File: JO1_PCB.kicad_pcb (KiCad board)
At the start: 2 copper layers, 118.1 x 90.2 mm, 5 parts, among them J1 Conn_02x10_Row_Letter_First, J2 Conn_02x08_Row_Letter_First, J3 Conn_02x15_Row_Letter_First, J4 Conn_02x17_Row_Letter_First

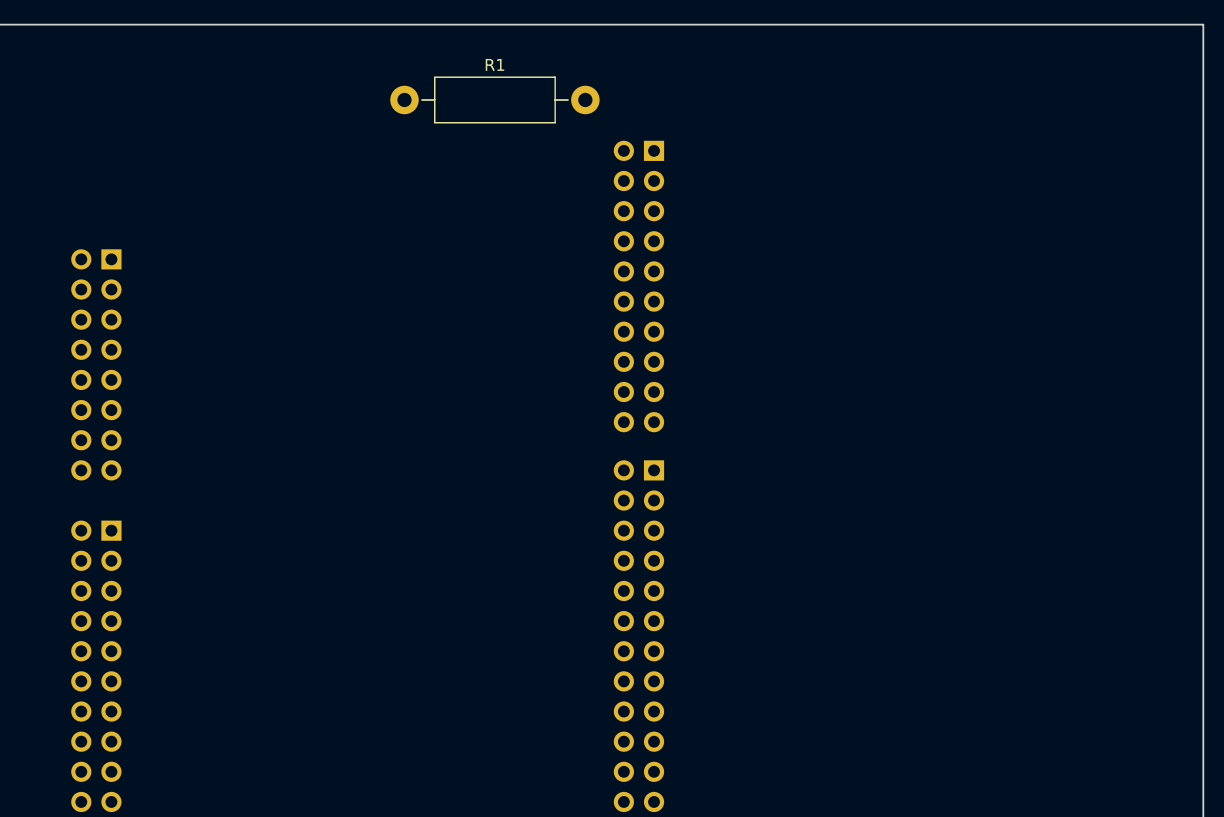
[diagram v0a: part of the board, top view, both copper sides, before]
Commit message: Added several components to the schematic
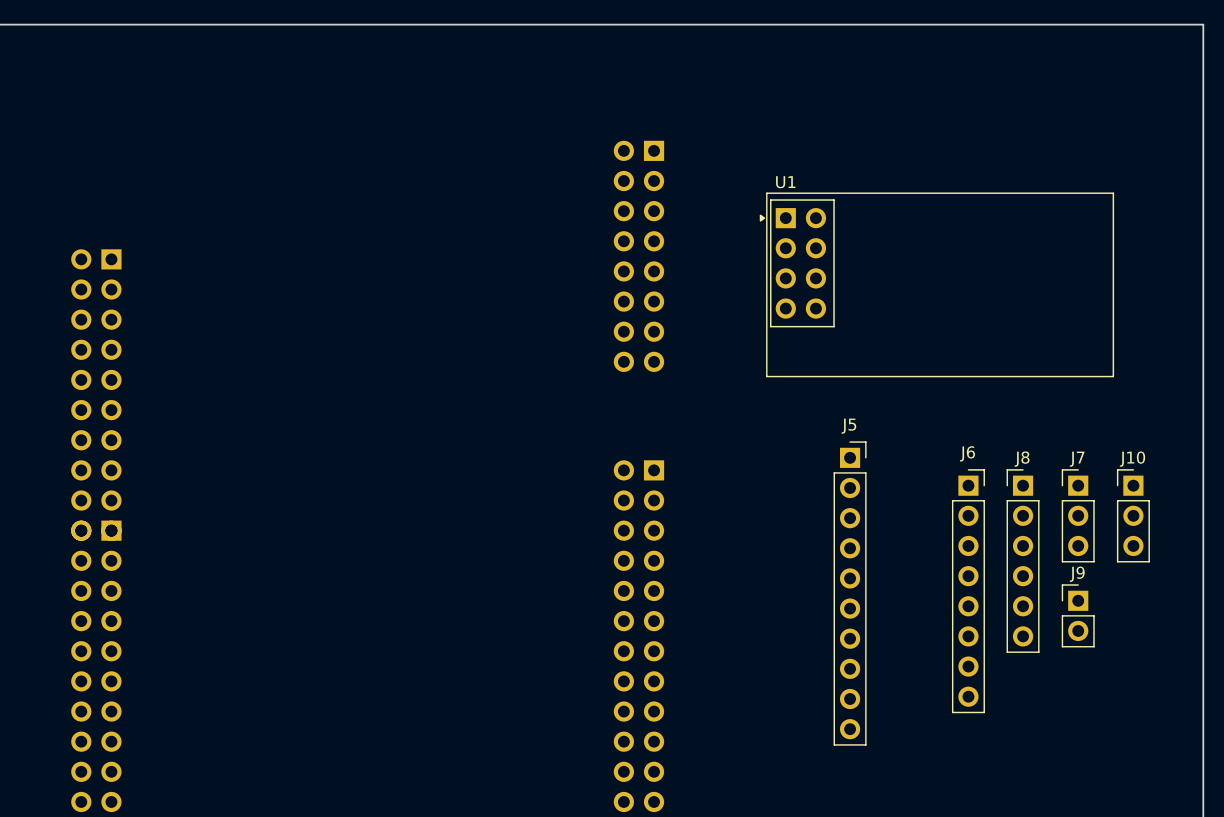
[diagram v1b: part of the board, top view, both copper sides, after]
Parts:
- removed R1: R, Resistor_THT:R_Axial_DIN0411_L9.9mm_D3.6mm_P15.24mm_Horizontal
- added J10: ESC_PWM, Connector_PinHeader_2.54mm:PinHeader_1x03_P2.54mm_Vertical, F.Cu at (193.5, 90.9)
- added J5: MPU-6050, Connector_PinSocket_2.54mm:PinSocket_1x10_P2.54mm_Vertical, F.Cu at (169.6, 88.6)
- added J6: NUCLEO_WCMCU-1051, Connector_PinSocket_2.54mm:PinSocket_1x08_P2.54mm_Vertical, F.Cu at (179.6, 90.9)
- added J7: SERVO, Connector_PinHeader_2.54mm:PinHeader_1x03_P2.54mm_Vertical, F.Cu at (188.8, 90.9)
- added J8: DC_MOTOR, Connector_PinHeader_2.54mm:PinHeader_1x06_P2.54mm_Vertical, F.Cu at (184.2, 90.9)
- added J9: ESC_MOTOR, Connector_PinHeader_2.54mm:PinHeader_1x02_P2.54mm_Vertical, F.Cu at (188.8, 100.6)
- added U1: NRF24L01, RF_Module:nRF24L01_Breakout, F.Cu at (164.2, 68.4)
- J1: value Conn_02x10_Row_Letter_First -> CN8; footprint Connector_PinHeader_2.54mm:PinHeader_2x10_P2.54mm_Vertical -> Connector_PinHeader_2.54mm:PinHeader_2x08_P2.54mm_Vertical
- J2: value Conn_02x08_Row_Letter_First -> CN7; footprint Connector_PinHeader_2.54mm:PinHeader_2x08_P2.54mm_Vertical -> Connector_PinHeader_2.54mm:PinHeader_2x10_P2.54mm_Vertical
- J3: value Conn_02x15_Row_Letter_First -> CN9
- J4: value Conn_02x17_Row_Letter_First -> CN10
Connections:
- J3 pad GND: (no net) -> unconnected-(J3-12-PadGND)
- J3 pad PA3: (no net) -> unconnected-(J3-1-PadPA3)
- J3 pad PB1: (no net) -> unconnected-(J3-7-PadPB1)
- J3 pad PB14: (no net) -> unconnected-(J3-29-PadPB14)
- J3 pad PB2: (no net) -> unconnected-(J3-13-PadPB2)
- J3 pad PB5: (no net) -> unconnected-(J3-17-PadPB5)
- J3 pad PC0: (no net) -> unconnected-(J3-3-PadPC0)
- J3 pad PC2: (no net) -> unconnected-(J3-9-PadPC2)
- J3 pad PC3: (no net) -> unconnected-(J3-5-PadPC3)
- J3 pad PD0: (no net) -> NUCLEO_FDCAN_RX
- J3 pad PD1: (no net) -> NUCLEO_FDCAN_TX
- J3 pad PD10: (no net) -> unconnected-(J3-30-PadPD10)
- J3 pad PD3: (no net) -> unconnected-(J3-10-PadPD3)
- J3 pad PD4: (no net) -> unconnected-(J3-8-PadPD4)
- J3 pad PD5: (no net) -> unconnected-(J3-6-PadPD5)
- J3 pad PD6: (no net) -> unconnected-(J3-4-PadPD6)
- J3 pad PD7: (no net) -> unconnected-(J3-2-PadPD7)
- J3 pad PE2: (no net) -> unconnected-(J3-14-PadPE2)
- J3 pad PE3: (no net) -> unconnected-(J3-22-PadPE3)
- J3 pad PE4: (no net) -> unconnected-(J3-16-PadPE4)
- J3 pad PE5: (no net) -> unconnected-(J3-18-PadPE5)
- J3 pad PE6: (no net) -> unconnected-(J3-20-PadPE6)
- J3 pad PE9: (no net) -> unconnected-(J3-15-PadPE9)
- J3 pad PF11: (no net) -> NRF_SPI5_MOSI
- J3 pad PF14: (no net) -> IMU_I2C4_SCL
- J3 pad PF15: (no net) -> IMU_I2C4_SDA
- J3 pad PF7: (no net) -> NRF_SPI5_SCK
- J3 pad PF8: (no net) -> NRF_SPI5_MISO
- J3 pad PF9: (no net) -> ESC_TIM14_CH1
- J4 pad AGND: (no net) -> unconnected-(J4-3-PadAGND)
- J4 pad GND: (no net) -> unconnected-(J4-5-PadGND)
- J4 pad PA0: (no net) -> unconnected-(J4-29-PadPA0)
- J4 pad PA2: (no net) -> unconnected-(J4-11-PadPA2)
- J4 pad PA8: (no net) -> unconnected-(J4-4-PadPA8)
- J4 pad PB0: (no net) -> unconnected-(J4-31-PadPB0)
- J4 pad PB10: (no net) -> unconnected-(J4-32-PadPB10)
- J4 pad PB11: (no net) -> unconnected-(J4-34-PadPB11)
- J4 pad PB2: (no net) -> unconnected-(J4-15-PadPB2)
- J4 pad PB6: (no net) -> unconnected-(J4-14-PadPB6)
- J4 pad PB7: (no net) -> unconnected-(J4-16-PadPB7)
- J4 pad PD11: (no net) -> unconnected-(J4-23-PadPD11)
- J4 pad PD12: (no net) -> unconnected-(J4-21-PadPD12)
- J4 pad PD13: (no net) -> unconnected-(J4-19-PadPD13)
- J4 pad PE0: (no net) -> unconnected-(J4-33-PadPE0)
- J4 pad PE10: (no net) -> unconnected-(J4-24-PadPE10)
- J4 pad PE11: (no net) -> unconnected-(J4-6-PadPE11)
- J4 pad PE12: (no net) -> unconnected-(J4-26-PadPE12)
- J4 pad PE13: (no net) -> unconnected-(J4-10-PadPE13)
- J4 pad PE14: (no net) -> unconnected-(J4-8-PadPE14)
- J4 pad PE15: (no net) -> unconnected-(J4-30-PadPE15)
- J4 pad PE2: (no net) -> unconnected-(J4-25-PadPE2)
- J4 pad PE6: (no net) -> unconnected-(J4-28-PadPE6)
- J4 pad PE7: (no net) -> unconnected-(J4-20-PadPE7)
- J4 pad PE8: (no net) -> unconnected-(J4-18-PadPE8)
- J4 pad PG12: (no net) -> unconnected-(J4-2-PadPG12)
- J4 pad PG14: (no net) -> unconnected-(J4-12-PadPG14)
- J4 pad PG6: (no net) -> unconnected-(J4-13-PadPG6)
- J4 pad VDDA: (no net) -> unconnected-(J4-1-PadVDDA)

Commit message: avances.........
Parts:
- added J11: CAN_WCMCU-1051, Connector_PinSocket_2.54mm:PinSocket_1x08_P2.54mm_Vertical, F.Cu at (125.4, 132.1)
- added U2: BP, footprints:blue_pill, F.Cu at (137.8, 81.9)
- J6: value NUCLEO_WCMCU-1051 -> CAN_WCMCU-1051
- moved J8 84.2 mm to (115.6, 139.7), turned to 90 degrees
- moved J10 77.6 mm to (121.9, 61.0), turned to 180 degrees
- moved J9 60.8 mm to (142.2, 139.7), turned to 90 degrees
- moved U1 59.9 mm to (105.4, 57.1), turned to 90 degrees
- moved J6 51.5 mm to (133.7, 114.3)
- moved J5 48.9 mm to (218.4, 86.4)
- moved J1 46.6 mm to (107.4, 71.9)
- moved J2 46.6 mm to (153.1, 62.7)
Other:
- board size 118.1 x 90.2 mm -> 52.1 x 90.2 mm

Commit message: Added CAN transceiver for Blue Pill
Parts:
- added R1: 120, Resistor_THT:R_Radial_Power_L13.0mm_W9.0mm_P5.00mm, F.Cu at (118.5, 99.0)
- J11: value CAN_WCMCU-1051 -> CAN_WCMCU-1051_BLUEPILL
- J6: value CAN_WCMCU-1051 -> CAN_WCMCU-1051_NUCLEO
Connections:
- net ENCODER_A renamed BLUEPILL_ENCODER_A
- net ENCODER_B renamed BLUEPILL_ENCODER_B
- net ESC_TIM14_CH1 renamed NUCLEO_ESC_TIM14_CH1
- net IMU_I2C4_SCL renamed NUCLEO_IMU_I2C4_SCL
- net IMU_I2C4_SDA renamed NUCLEO_IMU_I2C4_SDA
- net NRF_CE renamed NUCLEO_NRF_CE
- net NRF_CSN renamed NUCLEO_NRF_CSN
- net NRF_SPI5_MISO renamed NUCLEO_NRF_SPI5_MISO
- net NRF_SPI5_MOSI renamed NUCLEO_NRF_SPI5_MOSI
- net NRF_SPI5_SCK renamed NUCLEO_NRF_SPI5_SCK
- net SERVO_TIM13_CH1 renamed NUCLEO_SERVO_TIM13_CH1
- J11 pad 3: unconnected-(J11-CTX-Pad3) -> BLUEPILL_CAN_TX
- J11 pad 4: unconnected-(J11-CRX-Pad4) -> BLUEPILL_CAN_RX
- J11 pad 5: unconnected-(J11-CANH-Pad5) -> Net-(J11-CANH)
- J11 pad 6: unconnected-(J11-CANL-Pad6) -> Net-(J11-CANL)
- J6 pad 5: unconnected-(J6-CANH-Pad5) -> Net-(J6-CANH)
- J6 pad 6: unconnected-(J6-CANL-Pad6) -> Net-(J6-CANL)
- U2 pad PA11: unconnected-(U2-PadPA11) -> BLUEPILL_CAN_RX
- U2 pad PA12: unconnected-(U2-PadPA12) -> BLUEPILL_CAN_TX

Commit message: Placed components
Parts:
- added H1: MountingHole, MountingHole:MountingHole_2.1mm, F.Cu at (103.5, 55.0)
- added H2: MountingHole, MountingHole:MountingHole_2.1mm, F.Cu at (157.5, 55.0)
- added H3: MountingHole, MountingHole:MountingHole_2.1mm, F.Cu at (103.5, 139.0)
- added H4: MountingHole, MountingHole:MountingHole_2.1mm, F.Cu at (157.5, 139.0)
- added R2: 120, Resistor_THT:R_Axial_DIN0204_L3.6mm_D1.6mm_P5.08mm_Horizontal, F.Cu at (129.2, 130.7)
- R1: footprint Resistor_THT:R_Radial_Power_L13.0mm_W9.0mm_P5.00mm -> Resistor_THT:R_Axial_DIN0204_L3.6mm_D1.6mm_P5.08mm_Horizontal
- moved J5 104.9 mm to (113.6, 89.6)
- moved J8 86.3 mm to (125.7, 54.0), turned to -90 degrees
- moved J9 86.2 mm to (133.0, 54.0), turned to -90 degrees
- moved J10 75.5 mm to (114.0, 136.0)
- moved J7 36.6 mm to (158.5, 70.5)
- moved R1 31.1 mm to (129.2, 128.2), turned to 180 degrees
- moved U1 28.2 mm to (113.9, 84.0)
- moved J11 16.7 mm to (134.0, 117.8), turned to 0 degrees
- moved J6 14.7 mm to (119.5, 117.8)
- moved U2 9.09 mm to (137.3, 91.0)
- moved J1 1.95 mm to (109.3, 72.1)
- moved J2 1.95 mm to (155.0, 62.9)
- moved J3 1.95 mm to (109.3, 94.9)
- moved J4 1.95 mm to (155.0, 89.9)
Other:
- board size 52.1 x 90.2 mm -> 60 x 90 mm

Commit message: Added screw terminals
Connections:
- J1 pad GND: GND -> unconnected-(J1-11-PadGND)
- J11 pad 1: unconnected-(J11-VCC-Pad1) -> 5V
- J5 pad 1: unconnected-(J5-VCC-Pad1) -> 5V
- J6 pad 1: unconnected-(J6-VCC-Pad1) -> 5V
- J7 pad 2: unconnected-(J7-VCC-Pad2) -> 5V
- J8 pad 4: unconnected-(J8-ENCODER_VCC-Pad4) -> 5V
- U1 pad 2: unconnected-(U1-VCC-Pad2) -> 3.3V

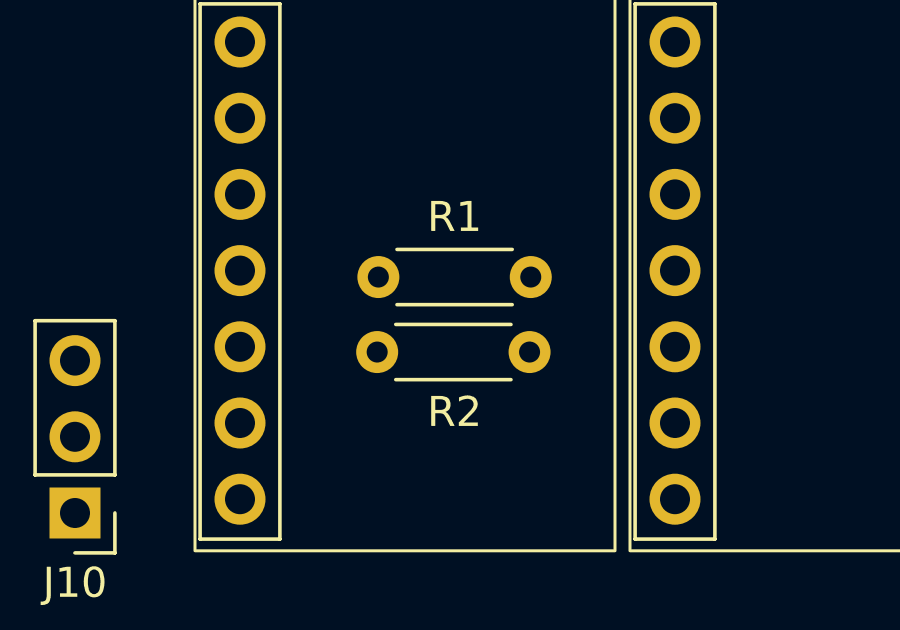
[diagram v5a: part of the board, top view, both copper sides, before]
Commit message: Corrected CAN bus
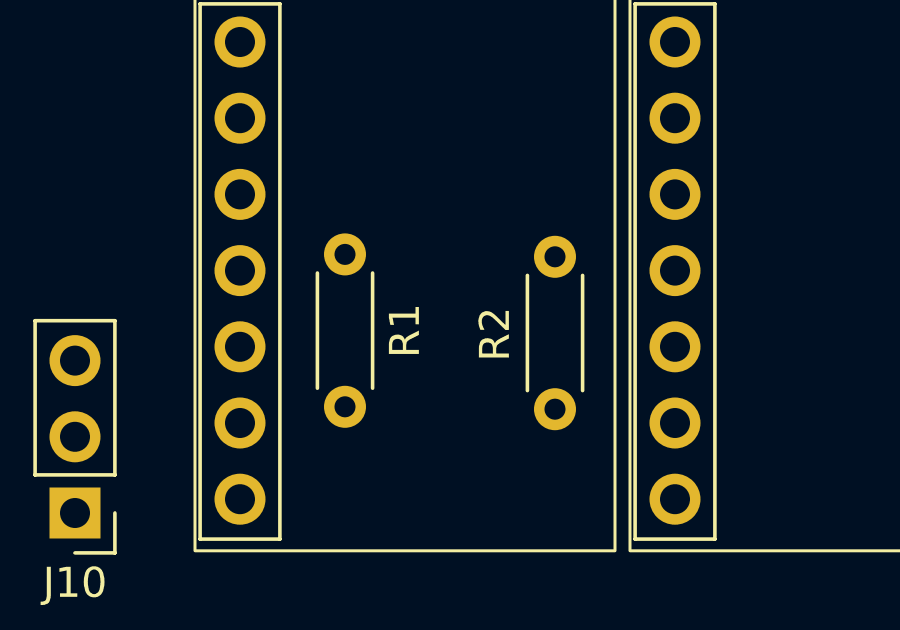
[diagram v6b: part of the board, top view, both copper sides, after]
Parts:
- moved R1 7.55 mm to (123.0, 132.5), turned to 90 degrees
- moved R2 2.09 mm to (130.0, 132.6), turned to 90 degrees
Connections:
- J6 pad 5: Net-(J6-CANH) -> Net-(J11-CANH)
- J6 pad 6: Net-(J6-CANL) -> Net-(J11-CANL)
- R1 pad 1: Net-(J11-CANH) -> Net-(J11-CANL)
- R1 pad 2: Net-(J6-CANH) -> Net-(J11-CANH)
- R2 pad 2: Net-(J6-CANL) -> Net-(J11-CANH)

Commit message: Routing
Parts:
- added J12: TFT, Connector_PinSocket_2.54mm:PinSocket_1x09_P2.54mm_Vertical, F.Cu at (125.5, 100.7)
- added J13: LM2596_3.3V, TerminalBlock_MetzConnect:TerminalBlock_MetzConnect_Type094_RT03502HBLU_1x02_P5.00mm_Horizontal, F.Cu at (117.0, 48.0)
- added J14: LM2596_5V, TerminalBlock_MetzConnect:TerminalBlock_MetzConnect_Type094_RT03502HBLU_1x02_P5.00mm_Horizontal, F.Cu at (149.0, 47.8)
- moved H2 59.6 mm to (98.5, 46.5)
- moved H4 59.2 mm to (98.5, 134.5)
- moved H1 56.1 mm to (159.0, 46.5)
- moved H3 55.7 mm to (159.0, 134.5)
- moved U1 31.9 mm to (99.7, 55.4), turned to 0 degrees
- moved J5 25.2 mm to (103.0, 112.5)
- moved J8 11.3 mm to (136.1, 49.5)
- moved J9 8.51 mm to (133.5, 45.5), turned to 90 degrees
- moved J10 5.81 mm to (119.0, 133.1)
- moved R1 4.03 mm to (127.0, 132.0)
- moved J6 3.50 mm to (123.0, 117.6)
- moved J11 3.39 mm to (137.4, 117.6)
- moved R2 3.05 mm to (133.0, 132.0)
- moved U2 2.25 mm to (137.3, 88.7)
- moved J7 0.50 mm to (159.0, 70.5)
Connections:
- J1 pad GND: unconnected-(J1-11-PadGND) -> GND
- J2 pad GND: unconnected-(J2-8-PadGND) -> GND
- J3 pad GND: unconnected-(J3-12-PadGND) -> GND
- J4 pad GND: unconnected-(J4-5-PadGND) -> GND
- U2 pad 3V3: unconnected-(U2-3.3V-Pad3V3) -> 3.3V
- U2 pad G: unconnected-(U2-GND-PadG) -> GND
- U2 pad PA0: unconnected-(U2-PadPA0) -> BLUEPILL_ENCODER_A
- U2 pad PA1: unconnected-(U2-PadPA1) -> BLUEPILL_ENCODER_B
- U2 pad PA4: unconnected-(U2-PadPA4) -> BLUEPILL_TFT_RESET
- U2 pad PA5: unconnected-(U2-PadPA5) -> BLUEPILL_TFT_CLK
- U2 pad PA6: unconnected-(U2-PadPA6) -> BLUEPILL_TFT_DC
- U2 pad PA7: unconnected-(U2-PadPA7) -> BLUEPILL_TFT_MOSI
- U2 pad PB0: unconnected-(U2-PadPB0) -> BLUEPILL_TFT_CS
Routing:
- net NUCLEO_NRF_SPI5_SCK: track 0.00 -> 86.5 mm
- net 3.3V: track 0.00 -> 77.8 mm
- net NUCLEO_NRF_SPI5_MISO: track 0.00 -> 67.9 mm
- net NUCLEO_NRF_CSN: track 0.00 -> 63.7 mm
- net NUCLEO_NRF_CE: track 0.00 -> 62.5 mm
- net NUCLEO_NRF_SPI5_MOSI: track 0.00 -> 49.1 mm
- net NUCLEO_FDCAN_RX: track 0.00 -> 40.5 mm
- net BLUEPILL_CAN_TX: track 0.00 -> 39.0 mm
- net BLUEPILL_CAN_RX: track 0.00 -> 38.4 mm
- net NUCLEO_FDCAN_TX: track 0.00 -> 32.8 mm
- net BLUEPILL_ENCODER_B: track 0.00 -> 28.0 mm
- net BLUEPILL_TFT_CLK: track 0.00 -> 27.1 mm
- net BLUEPILL_ENCODER_A: track 0.00 -> 24.5 mm
- net GND: track 0.00 -> 18.4 mm
- net NUCLEO_ESC_TIM14_CH1: track 0.00 -> 10.3 mm
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- added copper zone on B.Cu, net 5V
- added copper zone on F.Cu, net GND
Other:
- board size 60 x 90 mm -> 66.5 x 94 mm

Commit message: ya mero casi
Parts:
- added C1: 100nF, Capacitor_THT:C_Disc_D4.7mm_W2.5mm_P5.00mm, F.Cu at (159.3, 61.3)
- added R3: 1K, Resistor_THT:R_Axial_DIN0207_L6.3mm_D2.5mm_P10.16mm_Horizontal, F.Cu at (129.3, 55.6)
- added SW1: SW_Nidec_CAS-120A1, Button_Switch_THT:SW_Slide-03_Wuerth-WS-SLTV_10x2.5x6.4_P2.54mm, F.Cu at (157.2, 54.6)
- R1, R2: footprint Resistor_THT:R_Axial_DIN0204_L3.6mm_D1.6mm_P5.08mm_Horizontal -> Resistor_THT:R_Axial_DIN0207_L6.3mm_D2.5mm_P10.16mm_Horizontal
- moved R1 19.1 mm to (146.1, 132.1)
- moved R2 19.0 mm to (114.0, 131.6)
- moved J10 1.77 mm to (118.1, 134.6), turned to -90 degrees
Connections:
- net Net-(J11-CANH) renamed CAN_+
- net Net-(J11-CANL) renamed CAN_-
- J2 pad PB8: unconnected-(J2-2-PadPB8) -> Net-(J2-2)
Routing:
- net CAN_-: track 0.00 -> 39.7 mm
- net CAN_+: track 0.00 -> 37.9 mm
- net (no net): track 0.00 -> 19.3 mm
- net Net-(J2-2): track 0.00 -> 14.8 mm
- net 3.3V: track 77.8 -> 89.9 mm
- net GND: track 18.4 -> 21.7 mm
- net NUCLEO_FDCAN_TX: track 32.8 -> 35.3 mm
- net NUCLEO_NRF_CE: track 62.5 -> 64.5 mm
- net NUCLEO_ESC_TIM14_CH1: track 10.3 -> 8.79 mm
